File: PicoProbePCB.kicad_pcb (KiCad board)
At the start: 2 copper layers, 68.6 x 81.3 mm, 3 parts, among them J1 Conn_01x03_Socket, U1 RaspberryPi_Pico_SecondaryPins, U2 RaspberryPi_Pico

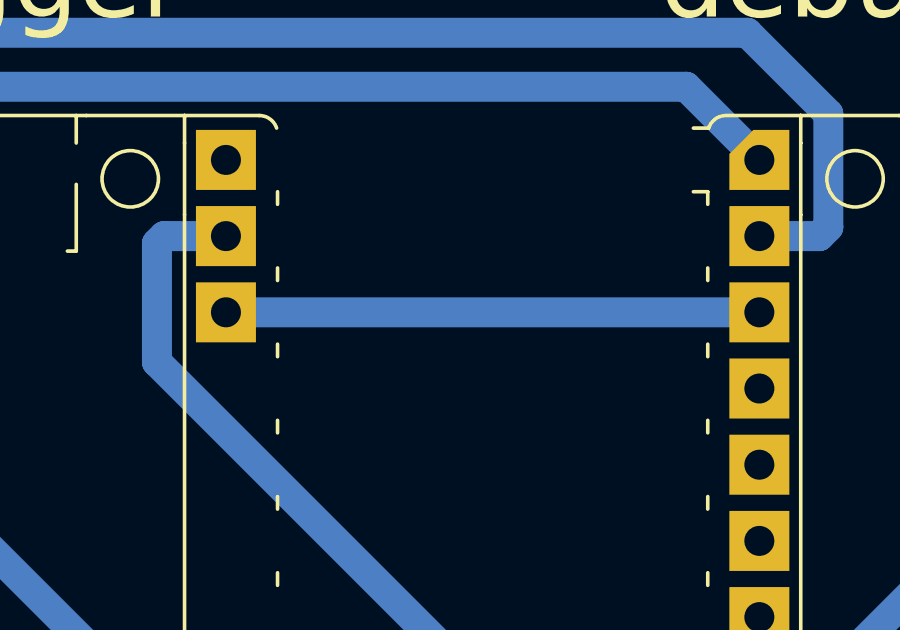
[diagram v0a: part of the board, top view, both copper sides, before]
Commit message: add optional smt power led on top layer
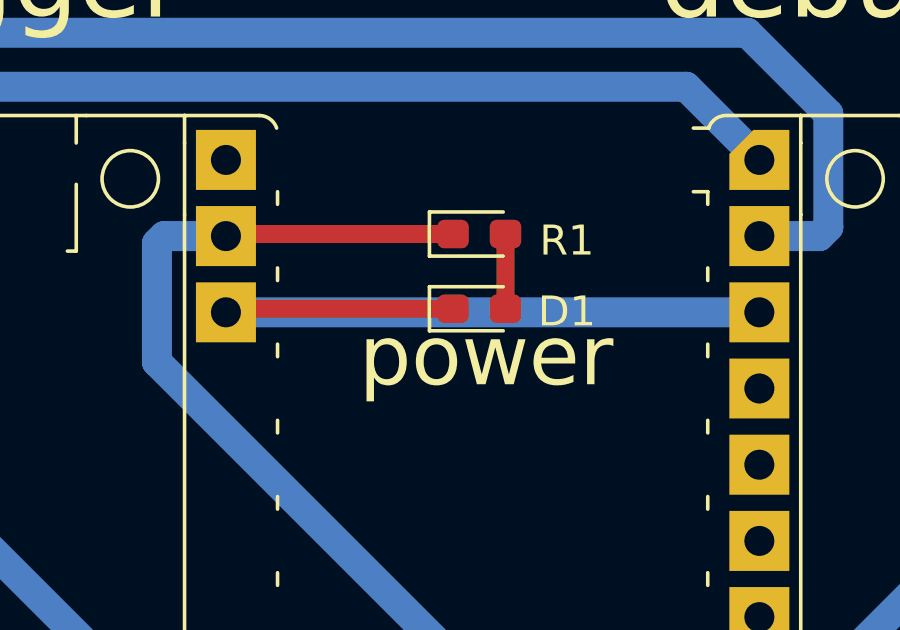
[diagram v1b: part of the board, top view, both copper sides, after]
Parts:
- added D1: LED, LED_SMD:LED_0603_1608Metric_Pad1.05x0.95mm_HandSolder, F.Cu at (191.5, 80.6)
- added R1: R, LED_SMD:LED_0603_1608Metric_Pad1.05x0.95mm_HandSolder, F.Cu at (191.5, 78.1)
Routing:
- net GND: track 91.8 -> 99.4 mm
- net VCC: track 55.6 -> 63.2 mm
- net Net-(D1-A): track 0.00 -> 2.49 mm
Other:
- board text added: "power"
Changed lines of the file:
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@@
   (net 16 "unconnected-(U2-GPIO0-Pad1)")
   (net 17 "unconnected-(U2-GPIO1-Pad2)")
-  (net 18 "unconnected-(U2-GPIO14-Pad19)")
-  (net 19 "unconnected-(U2-GPIO15-Pad20)")
-  (net 20 "unconnected-(U2-GPIO16-Pad21)")
-  (net 21 "unconnected-(U2-GPIO17-Pad22)")
-  (net 22 "unconnected-(U2-VBUS-Pad40)")
+  (net 18 "Net-(D1-A)")
+  (net 19 "unconnected-(U2-GPIO14-Pad19)")
+  (net 20 "unconnected-(U2-GPIO15-Pad20)")
+  (net 21 "unconnected-(U2-GPIO16-Pad21)")
+  (net 22 "unconnected-(U2-GPIO17-Pad22)")
+  (net 23 "unconnected-(U2-VBUS-Pad40)")
+  (footprint "LED_SMD:LED_0603_1608Metric_Pad1.05x0.95mm_HandSolder" (layer "F.Cu")
+    (at 191.458 80.551)
+    (descr "LED SMD 0603 (1608 Metric), square (rectangular) end terminal, IPC_7351 nominal, (Body size source: http://www.tortai-tech.com/upload/download/2011102023233369053.pdf), generated with kicad-footprint-generator")
+    (tags "LED handsolder")
+    (property "Sheetfile" "PicoProbePCB.kicad_sch")
+    (property "Sheetname" "")
+    (property "ki_description" "Light emitting diode")
+    (property "ki_keywords" "LED diode")
+    (attr smd)
+    (fp_text reference "D1" (at 2.921 0.094) (layer "F.SilkS")
+        (effects (font (size 1 1) (thickness 0.15)))
+    )
+    (fp_text value "LED" (at 0 1.43) (layer "F.Fab")
+        (effects (font (size 1 1) (thickness 0.15)))
+    )
+    (fp_text user "${REFERENCE}" (at 0 0) (layer "F.Fab")
+        (effects (font (size 0.4 0.4) (thickness 0.06)))
+    )
+    (fp_line (start -1.66 -0.735) (end -1.66 0.735)
+      (stroke (width 0.12) (type solid)) (layer "F.SilkS"))
+    (fp_line (start -1.66 0.735) (end 0.8 0.735)
+      (stroke (width 0.12) (type solid)) (layer "F.SilkS"))
+    (fp_line (start 0.8 -0.735) (end -1.66 -0.735)
+      (stroke (width 0.12) (type solid)) (layer "F.SilkS"))
+    (fp_line (start -1.65 -0.73) (end 1.65 -0.73)
+      (stroke (width 0.05) (type solid)) (layer "F.CrtYd"))
+    (fp_line (start -1.65 0.73) (end -1.65 -0.73)
+      (stroke (width 0.05) (type solid)) (layer "F.CrtYd"))
+    (fp_line (start 1.65 -0.73) (end 1.65 0.73)
+      (stroke (width 0.05) (type solid)) (layer "F.CrtYd"))
+    (fp_line (start 1.65 0.73) (end -1.65 0.73)
+      (stroke (width 0.05) (type solid)) (layer "F.CrtYd"))
+    (fp_line (start -0.8 -0.1) (end -0.8 0.4)
+      (stroke (width 0.1) (type solid)) (layer "F.Fab"))
+    (fp_line (start -0.8 0.4) (end 0.8 0.4)
+      (stroke (width 0.1) (type solid)) (layer "F.Fab"))
+    (fp_line (start -0.5 -0.4) (end -0.8 -0.1)
+      (stroke (width 0.1) (type solid)) (layer "F.Fab"))
+    (fp_line (start 0.8 -0.4) (end -0.5 -0.4)
+      (stroke (width 0.1) (type solid)) (layer "F.Fab"))
+    (fp_line (start 0.8 0.4) (end 0.8 -0.4)
+      (stroke (width 0.1) (type solid)) (layer "F.Fab"))
+    (pad "1" smd roundrect (at -0.875 0) (size 1.05 0.95) (layers "F.Cu" "F.Paste" "F.Mask") (roundrect_rratio 0.25)
+      (net 2 "GND") (pinfunction "K") (pintype "passive"))
+    (pad "2" smd roundrect (at 0.875 0) (size 1.05 0.95) (layers "F.Cu" "F.Paste" "F.Mask") (roundrect_rratio 0.25)
+      (net 18 "Net-(D1-A)") (pinfunction "A") (pintype "passive"))
+    (model "${KICAD6_3DMODEL_DIR}/LED_SMD.3dshapes/LED_0603_1608Metric.wrl"
+      (offset (xyz 0 0 0))
+      (scale (xyz 1 1 1))
+      (rotate (xyz 0 0 0))
+    )
+  )
   (footprint "Module_RaspberryPi_Pico:RaspberryPi_Pico_Debug_PicoProbePinsOnlyLargePads" (layer "F.Cu")
     (at 174.125 99.72)
@@
       (net 2 "GND") (pinfunction "GND") (pintype "passive"))
     (pad "19" thru_hole rect (at -8.89 21.59) (size 2 2) (drill 1) (layers "*.Cu" "*.Mask")
-      (net 18 "unconnected-(U2-GPIO14-Pad19)") (pinfunction "GPIO14") (pintype "bidirectional"))
+      (net 19 "unconnected-(U2-GPIO14-Pad19)") (pinfunction "GPIO14") (pintype "bidirectional"))
     (pad "20" thru_hole rect (at -8.89 24.13) (size 2 2) (drill 1) (layers "*.Cu" "*.Mask")
-      (net 19 "unconnected-(U2-GPIO15-Pad20)") (pinfunction "GPIO15") (pintype "bidirectional"))
+      (net 20 "unconnected-(U2-GPIO15-Pad20)") (pinfunction "GPIO15") (pintype "bidirectional"))
     (pad "21" thru_hole rect (at 8.89 24.13) (size 2 2) (drill 1) (layers "*.Cu" "*.Mask")
-      (net 20 "unconnected-(U2-GPIO16-Pad21)") (pinfunction "GPIO16") (pintype "bidirectional"))
+      (net 21 "unconnected-(U2-GPIO16-Pad21)") (pinfunction "GPIO16") (pintype "bidirectional"))
     (pad "22" thru_hole rect (at 8.89 21.59) (size 2 2) (drill 1) (layers "*.Cu" "*.Mask")
-      (net 21 "unconnected-(U2-GPIO17-Pad22)") (pinfunction "GPIO17") (pintype "bidirectional"))
+      (net 22 "unconnected-(U2-GPIO17-Pad22)") (pinfunction "GPIO17") (pintype "bidirectional"))
     (pad "23" thru_hole rect (at 8.89 19.05) (size 2 2) (drill 1) (layers "*.Cu" "*.Mask")
       (net 2 "GND") (pinfunction "GND") (pintype "passive"))
@@
       (net 14 "VCC") (pinfunction "VSYS") (pintype "power_in"))
     (pad "40" thru_hole rect (at 8.89 -24.13) (size 2 2) (drill 1) (layers "*.Cu" "*.Mask")
-      (net 22 "unconnected-(U2-VBUS-Pad40)") (pinfunction "VBUS") (pintype "power_out"))
+      (net 23 "unconnected-(U2-VBUS-Pad40)") (pinfunction "VBUS") (pintype "power_out"))
     (pad "D1" thru_hole rect (at -2.54 24.13) (size 2 2) (drill 1) (layers "*.Cu" "*.Mask"))
     (pad "D2" thru_hole rect (at 0 24.13) (size 2 2) (drill 1) (layers "*.Cu" "*.Mask"))
@@
     )
   )
+  (footprint "LED_SMD:LED_0603_1608Metric_Pad1.05x0.95mm_HandSolder" (layer "F.Cu")
+    (at 191.458 78.061)
+    (descr "LED SMD 0603 (1608 Metric), square (rectangular) end terminal, IPC_7351 nominal, (Body size source: http://www.tortai-tech.com/upload/download/2011102023233369053.pdf), generated with kicad-footprint-generator")
+    (tags "LED handsolder")
+    (property "Sheetfile" "PicoProbePCB.kicad_sch")
+    (property "Sheetname" "")
+    (property "ki_description" "Resistor")
+    (property "ki_keywords" "R res resistor")
+    (attr smd)
+    (fp_text reference "R1" (at 2.921 0.221) (layer "F.SilkS")
+        (effects (font (size 1 1) (thickness 0.15)))
+    )
+    (fp_text value "R" (at 0 1.43) (layer "F.Fab")
+        (effects (font (size 1 1) (thickness 0.15)))
+    )
+    (fp_text user "${REFERENCE}" (at 0 0) (layer "F.Fab")
+        (effects (font (size 0.4 0.4) (thickness 0.06)))
+    )
+    (fp_line (start -1.66 -0.735) (end -1.66 0.735)
+      (stroke (width 0.12) (type solid)) (layer "F.SilkS"))
+    (fp_line (start -1.66 0.735) (end 0.8 0.735)
+      (stroke (width 0.12) (type solid)) (layer "F.SilkS"))
+    (fp_line (start 0.8 -0.735) (end -1.66 -0.735)
+      (stroke (width 0.12) (type solid)) (layer "F.SilkS"))
+    (fp_line (start -1.65 -0.73) (end 1.65 -0.73)
+      (stroke (width 0.05) (type solid)) (layer "F.CrtYd"))
+    (fp_line (start -1.65 0.73) (end -1.65 -0.73)
+      (stroke (width 0.05) (type solid)) (layer "F.CrtYd"))
+    (fp_line (start 1.65 -0.73) (end 1.65 0.73)
+      (stroke (width 0.05) (type solid)) (layer "F.CrtYd"))
+    (fp_line (start 1.65 0.73) (end -1.65 0.73)
+      (stroke (width 0.05) (type solid)) (layer "F.CrtYd"))
+    (fp_line (start -0.8 -0.1) (end -0.8 0.4)
+      (stroke (width 0.1) (type solid)) (layer "F.Fab"))
+    (fp_line (start -0.8 0.4) (end 0.8 0.4)
+      (stroke (width 0.1) (type solid)) (layer "F.Fab"))
+    (fp_line (start -0.5 -0.4) (end -0.8 -0.1)
+      (stroke (width 0.1) (type solid)) (layer "F.Fab"))
+    (fp_line (start 0.8 -0.4) (end -0.5 -0.4)
+      (stroke (width 0.1) (type solid)) (layer "F.Fab"))
+    (fp_line (start 0.8 0.4) (end 0.8 -0.4)
+      (stroke (width 0.1) (type solid)) (layer "F.Fab"))
+    (pad "1" smd roundrect (at -0.875 0) (size 1.05 0.95) (layers "F.Cu" "F.Paste" "F.Mask") (roundrect_rratio 0.25)
+      (net 14 "VCC") (pintype "passive"))
+    (pad "2" smd roundrect (at 0.875 0) (size 1.05 0.95) (layers "F.Cu" "F.Paste" "F.Mask") (roundrect_rratio 0.25)
+      (net 18 "Net-(D1-A)") (pintype "passive"))
+    (model "${KICAD6_3DMODEL_DIR}/LED_SMD.3dshapes/LED_0603_1608Metric.wrl"
+      (offset (xyz 0 0 0))
+      (scale (xyz 1 1 1))
+      (rotate (xyz 0 0 0))
+    )
+  )
   (gr_rect (start 157.48 55.88) (end 226.06 137.16)
     (stroke (width 0.1) (type default)) (fill none) (layer "Edge.Cuts"))
+  (gr_text "power" (at 187.452 83.312) (layer "F.SilkS")
+    (effects (font (size 2 2) (thickness 0.15)) (justify left bottom))
+  )
   (gr_text "debugger" (at 165.1 71.12) (layer "F.SilkS")
     (effects (font (size 2.5 2.5) (thickness 0.2)) (justify left bottom))
@@
   (segment (start 207.145 120.52) (end 169.835 83.21) (width 1) (layer "B.Cu") (net 1))
   (segment (start 207.145 128.946) (end 207.184 128.985) (width 1) (layer "B.Cu") (net 1))
+  (segment (start 190.583 80.551) (end 183.134 80.551) (width 0.6) (layer "F.Cu") (net 2))
+  (segment (start 183.134 80.551) (end 183.015 80.67) (width 0.6) (layer "F.Cu") (net 2))
   (segment (start 209.685 120.515) (end 209.685 123.85) (width 1) (layer "B.Cu") (net 2))
   (segment (start 165.235 118.77) (end 183.015 118.77) (width 1) (layer "B.Cu") (net 2))
@@
   (segment (start 163.169416 90.83) (end 165.235 90.83) (width 1) (layer "B.Cu") (net 5))
   (segment (start 161.135 73.815) (end 161.135 88.795584) (width 1) (layer "B.Cu") (net 5))
+  (segment (start 183.084 78.061) (end 183.015 78.13) (width 0.6) (layer "F.Cu") (net 14))
+  (segment (start 190.583 78.061) (end 183.084 78.061) (width 0.6) (layer "F.Cu") (net 14))
   (segment (start 191.516 93.13) (end 202.78 93.13) (width 1) (layer "B.Cu") (net 14))
   (segment (start 180.715 78.37) (end 180.715 82.329) (width 1) (layer "B.Cu") (net 14))
@@
   (segment (start 216.154 78.491) (end 216.515 78.13) (width 1) (layer "B.Cu") (net 14))
   (segment (start 216.515 78.13) (end 218.575 78.13) (width 1) (layer "B.Cu") (net 14))
+  (segment (start 192.333 78.061) (end 192.333 80.551) (width 0.6) (layer "F.Cu") (net 18))
   (zone (net 2) (net_name "GND") (layer "B.Cu") (hatch edge 0.5)
     (connect_pads yes (clearance 0.5))

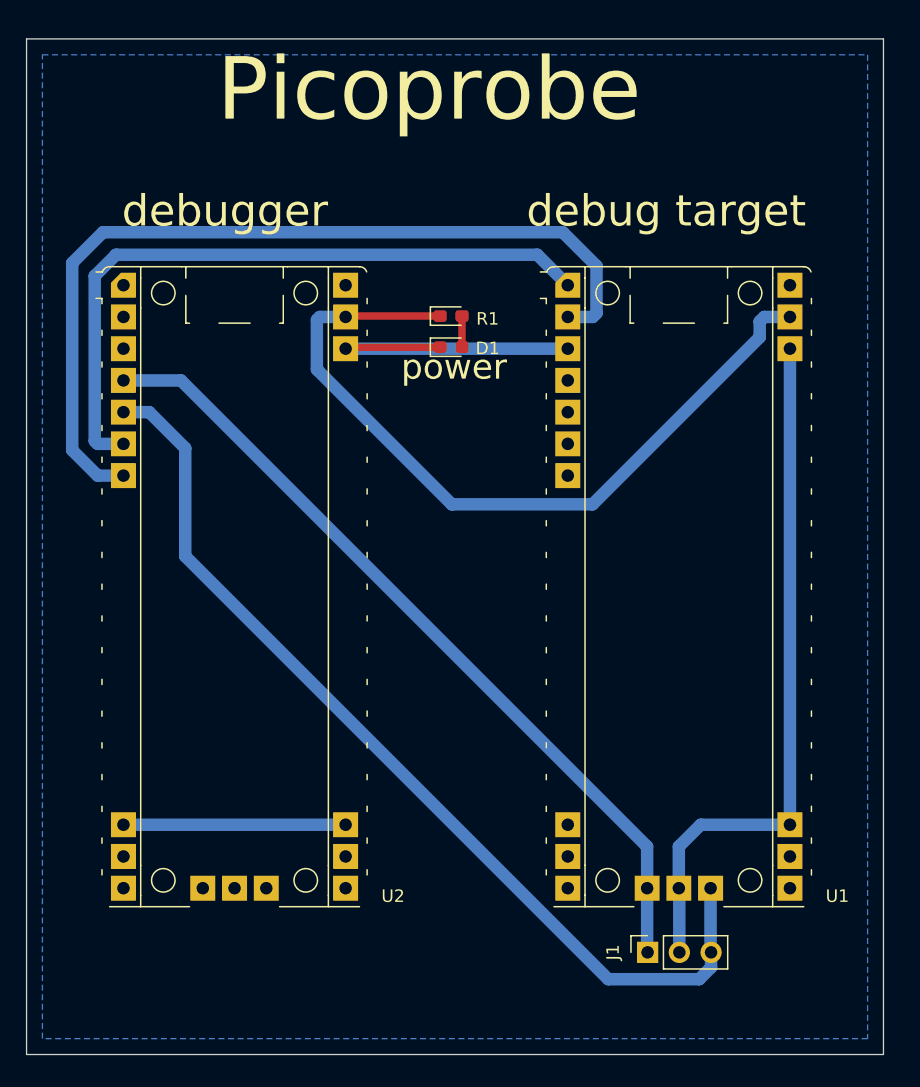
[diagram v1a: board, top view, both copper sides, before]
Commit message: update to kicad 8.0 and add top-layer (optional) power rail breakout
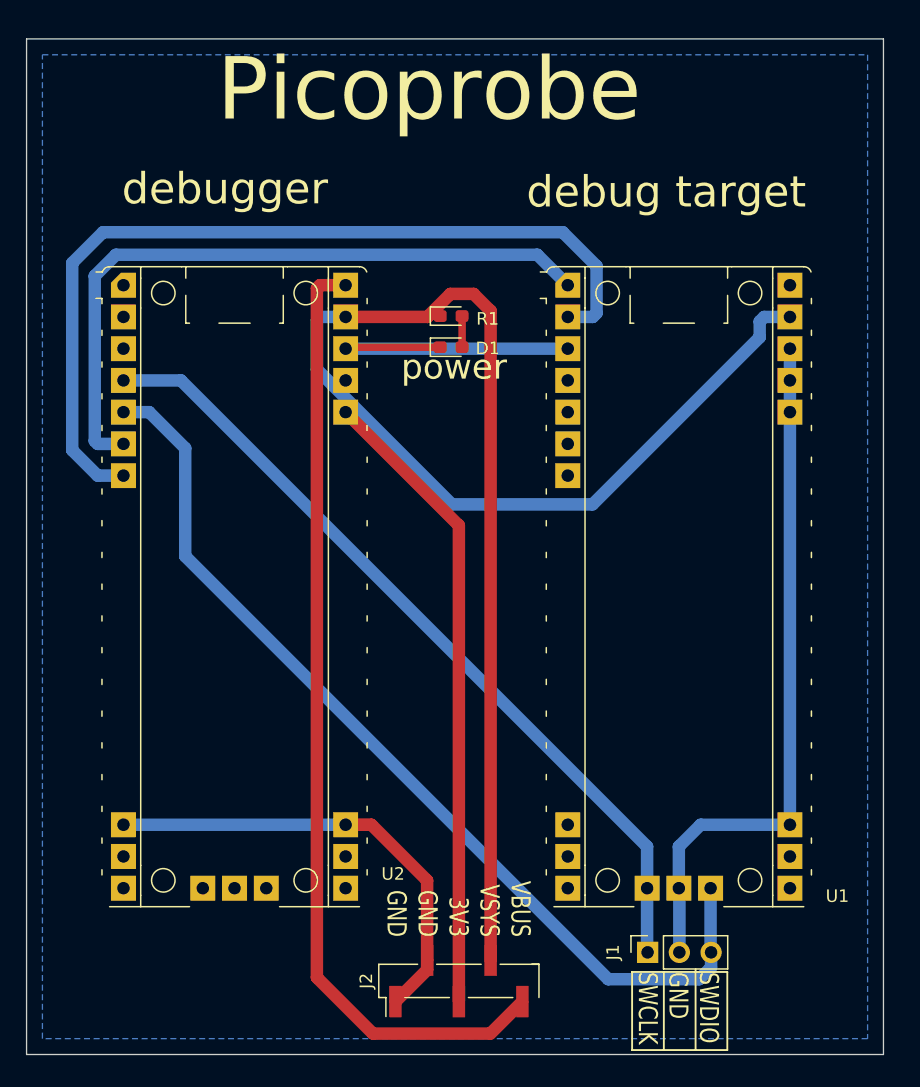
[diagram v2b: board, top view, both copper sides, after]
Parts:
- added J2: Conn_01x05, Connector_PinHeader_2.54mm:PinHeader_1x05_P2.54mm_Vertical_SMD_Pin1Left, F.Cu at (192.1, 131.3)
- U1, U2: footprint Module_RaspberryPi_Pico:RaspberryPi_Pico_Debug_PicoProbePinsOnlyLargePads -> RaspberryPi_Pico:RaspberryPi_Pico_Debug_PicoProbePinsOnlyLargePads
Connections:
- U2 pad 40: unconnected-(U2-VBUS-Pad40) -> VBUS
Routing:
- net VBUS: track 0.00 -> 76.9 mm
- net VCC: track 63.2 -> 128.1 mm
- net +3V3: track 0.00 -> 50.9 mm
- net GND: track 99.4 -> 118.5 mm
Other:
- board text added: "SWDIO GND SWCLK"
- board text added: "VBUS VSYS 3V3 GND GND"

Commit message: add photos and improve silkscreen for v2 board
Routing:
- net GND: track 118.5 -> 122.1 mm
- net VCC: track 128.1 -> 131.5 mm
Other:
- board text added: "Rev 2.0, 2024 Patrick Leiser Patronics.org"
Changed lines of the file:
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@@
 		)
 		(property "Value" "RaspberryPi_Pico"
-			(at 0 27.94 0)
+			(at -0.4064 16.2052 0)
 			(unlocked yes)
 			(layer "F.Fab")
@@
 		)
 		(property "Value" "RaspberryPi_Pico_SecondaryPins"
-			(at 0 27.94 0)
+			(at -0.254 14.5796 0)
 			(unlocked yes)
 			(layer "F.Fab")
@@
 	)
 	(gr_line
+		(start 157.4292 126.8984)
+		(end 176.53 126.8984)
+		(stroke
+			(width 0.15)
+			(type default)
+		)
+		(layer "F.SilkS")
+	)
+	(gr_line
+		(start 176.53 126.8984)
+		(end 176.53 137.16)
+		(stroke
+			(width 0.15)
+			(type default)
+		)
+		(layer "F.SilkS")
+	)
+	(gr_line
 		(start 211.024 130.315)
 		(end 211.0232 136.8044)
@@
 		)
 	)
+	(gr_text "Rev 2.0, 2024\nPatrick Leiser\nPatronics.org"
+		(at 159.6136 135.2804 0)
+		(layer "F.SilkS")
+		(effects
+			(font
+				(size 1.5 1.5)
+				(thickness 0.2)
+			)
+			(justify left bottom)
+		)
+	)
 	(gr_text "debug target"
 		(at 197.485 69.596 0)
@@
 	)
 	(segment
-		(start 209.685 120.515)
-		(end 209.685 123.85)
+		(start 218.575 80.67)
+		(end 220.635 80.67)
 		(width 1)
 		(layer "B.Cu")
@@
 	)
 	(segment
-		(start 165.235 118.77)
-		(end 183.015 118.77)
+		(start 221.488 115.857)
+		(end 218.575 118.77)
 		(width 1)
 		(layer "B.Cu")
@@
 	)
 	(segment
-		(start 218.575 80.67)
-		(end 218.575 118.77)
+		(start 221.488 81.523)
+		(end 221.488 115.857)
+		(width 1)
+		(layer "B.Cu")
+		(net 2)
+	)
+	(segment
+		(start 209.685 120.515)
+		(end 209.685 123.85)
+		(width 1)
+		(layer "B.Cu")
+		(net 2)
+	)
+	(segment
+		(start 165.235 118.77)
+		(end 183.015 118.77)
 		(width 1)
 		(layer "B.Cu")
@@
 	)
 	(segment
+		(start 220.635 80.67)
+		(end 221.488 81.523)
+		(width 1)
+		(layer "B.Cu")
+		(net 2)
+	)
+	(segment
 		(start 218.575 118.77)
 		(end 211.43 118.77)
@@
 	)
 	(segment
-		(start 191.516 93.13)
-		(end 202.78 93.13)
+		(start 216.154 79.756)
+		(end 216.154 78.491)
 		(width 1)
 		(layer "B.Cu")
@@
 	(segment
 		(start 180.715 78.37)
-		(end 180.715 82.329)
+		(end 180.715 88.05)
 		(width 1)
 		(layer "B.Cu")
@@
 	)
 	(segment
-		(start 202.78 93.13)
-		(end 216.154 79.756)
+		(start 183.015 78.13)
+		(end 180.955 78.13)
 		(width 1)
 		(layer "B.Cu")
@@
 	)
 	(segment
-		(start 216.154 79.756)
-		(end 216.154 78.491)
+		(start 180.715 88.05)
+		(end 185.795 93.13)
 		(width 1)
 		(layer "B.Cu")
@@
 	)
 	(segment
-		(start 180.955 78.13)
-		(end 180.715 78.37)
+		(start 216.515 78.13)
+		(end 218.575 78.13)
 		(width 1)
 		(layer "B.Cu")
@@
 	)
 	(segment
-		(start 183.015 78.13)
-		(end 180.955 78.13)
+		(start 185.795 93.13)
+		(end 202.78 93.13)
 		(width 1)
 		(layer "B.Cu")
@@
 	)
 	(segment
-		(start 180.715 82.329)
-		(end 191.516 93.13)
+		(start 216.154 78.491)
+		(end 216.515 78.13)
 		(width 1)
 		(layer "B.Cu")
@@
 	)
 	(segment
-		(start 216.154 78.491)
-		(end 216.515 78.13)
+		(start 202.78 93.13)
+		(end 216.154 79.756)
 		(width 1)
 		(layer "B.Cu")
@@
 	)
 	(segment
-		(start 216.515 78.13)
-		(end 218.575 78.13)
+		(start 180.955 78.13)
+		(end 180.715 78.37)
 		(width 1)
 		(layer "B.Cu")
